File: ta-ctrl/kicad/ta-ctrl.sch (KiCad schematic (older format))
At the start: 25 parts, among them J1 PinSocket_16_ctrl, J2 PinSocket_16_ctrl, J3 MountingHole_ctrl, J4 PinSocket_4_ctrl, J5 PinSocket_4_ctrl, J6 PinSocket_5_ctrl, J7 PinSocket_5_ctrl, U1 LSF0204, U2 LSF0204, U3 LSF0204

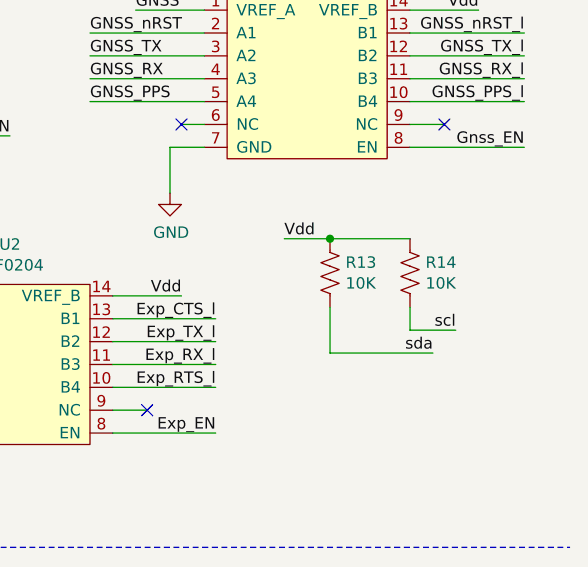
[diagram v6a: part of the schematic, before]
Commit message: updated parts vendors and added BOM
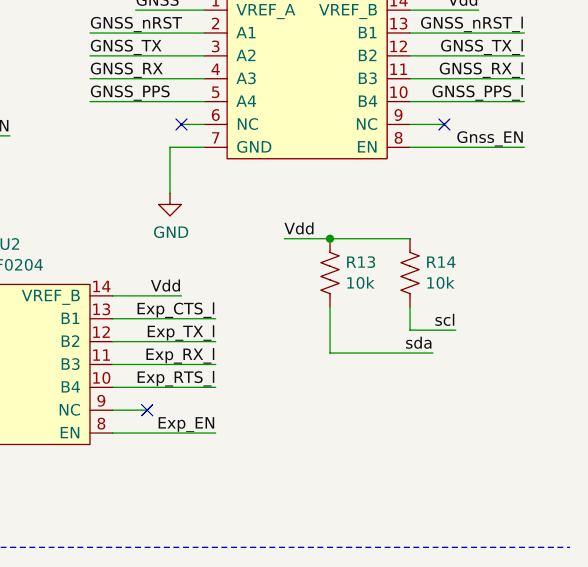
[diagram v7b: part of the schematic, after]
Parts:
- R13, R14: value 10K -> 10k; Manufacturer Part Number (none) -> CRCW060310K0FKEAHP; Vendor (none) -> Digikey; Vendor Part Number (none) -> 541-10.0KSCT-ND
- U1, U2, U3: Manufacturer Part Number (none) -> LSF0204QPWRQ1; Vendor (none) -> Digikey; Vendor Part Number (none) -> 296-51425-1-ND
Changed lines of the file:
@@
 F 2 "ta-ctrl:TSSOP-14" H 6850 1200 50  0001 C CNN
 F 3 "https://www.ti.com/lit/ds/symlink/lsf0204-q1.pdf?HQS=TI-null-null-digikeymode-df-pf-null-wwe&ts=1595462922658" H 6850 1200 50  0001 C CNN
+F 4 "LSF0204QPWRQ1" H 7050 1200 50  0001 C CNN "Manufacturer Part Number"
+F 5 "Digikey" H 7050 1200 50  0001 C CNN "Vendor"
+F 6 "296-51425-1-ND" H 7050 1200 50  0001 C CNN "Vendor Part Number"
 	1    7050 1200
 	1    0    0    -1
@@
 F 2 "ta-ctrl:TSSOP-14" H 9200 1250 50  0001 C CNN
 F 3 "https://www.ti.com/lit/ds/symlink/lsf0204-q1.pdf?HQS=TI-null-null-digikeymode-df-pf-null-wwe&ts=1595462922658" H 9200 1250 50  0001 C CNN
+F 4 "LSF0204QPWRQ1" H 9400 1250 50  0001 C CNN "Manufacturer Part Number"
+F 5 "Digikey" H 9400 1250 50  0001 C CNN "Vendor"
+F 6 "296-51425-1-ND" H 9400 1250 50  0001 C CNN "Vendor Part Number"
 	1    9400 1250
 	1    0    0    -1
@@
 F 2 "ta-ctrl:TSSOP-14" H 7900 2500 50  0001 C CNN
 F 3 "https://www.ti.com/lit/ds/symlink/lsf0204-q1.pdf?HQS=TI-null-null-digikeymode-df-pf-null-wwe&ts=1595462922658" H 7900 2500 50  0001 C CNN
+F 4 "LSF0204QPWRQ1" H 8100 2500 50  0001 C CNN "Manufacturer Part Number"
+F 5 "Digikey" H 8100 2500 50  0001 C CNN "Vendor"
+F 6 "296-51425-1-ND" H 8100 2500 50  0001 C CNN "Vendor Part Number"
 	1    8100 2500
 	1    0    0    -1
@@
 P 9500 2000
 F 0 "R13" H 9568 2046 50  0000 L CNN
-F 1 "10K" H 9568 1955 50  0000 L CNN
+F 1 "10k" H 9568 1955 50  0000 L CNN
 F 2 "ta-ctrl:R_0603_1608Metric_ctrl_cpy" V 9540 1990 50  0001 C CNN
-F 3 "~" H 9500 2000 50  0001 C CNN
+F 3 "https://www.digikey.com/product-detail/en/vishay-dale/CRCW060310K0FKEAHP/541-10-0KSCT-ND/2222780" H 9500 2000 50  0001 C CNN
+F 4 "CRCW060310K0FKEAHP" H 9500 2000 50  0001 C CNN "Manufacturer Part Number"
+F 5 "Digikey" H 9500 2000 50  0001 C CNN "Vendor"
+F 6 "541-10.0KSCT-ND" H 9500 2000 50  0001 C CNN "Vendor Part Number"
 	1    9500 2000
 	1    0    0    -1
@@
 P 9850 2000
 F 0 "R14" H 9918 2046 50  0000 L CNN
-F 1 "10K" H 9918 1955 50  0000 L CNN
+F 1 "10k" H 9918 1955 50  0000 L CNN
 F 2 "ta-ctrl:R_0603_1608Metric_ctrl_cpy" V 9890 1990 50  0001 C CNN
-F 3 "~" H 9850 2000 50  0001 C CNN
+F 3 "https://www.digikey.com/product-detail/en/vishay-dale/CRCW060310K0FKEAHP/541-10-0KSCT-ND/2222780" H 9850 2000 50  0001 C CNN
+F 4 "CRCW060310K0FKEAHP" H 9850 2000 50  0001 C CNN "Manufacturer Part Number"
+F 5 "Digikey" H 9850 2000 50  0001 C CNN "Vendor"
+F 6 "541-10.0KSCT-ND" H 9850 2000 50  0001 C CNN "Vendor Part Number"
 	1    9850 2000
 	1    0    0    -1

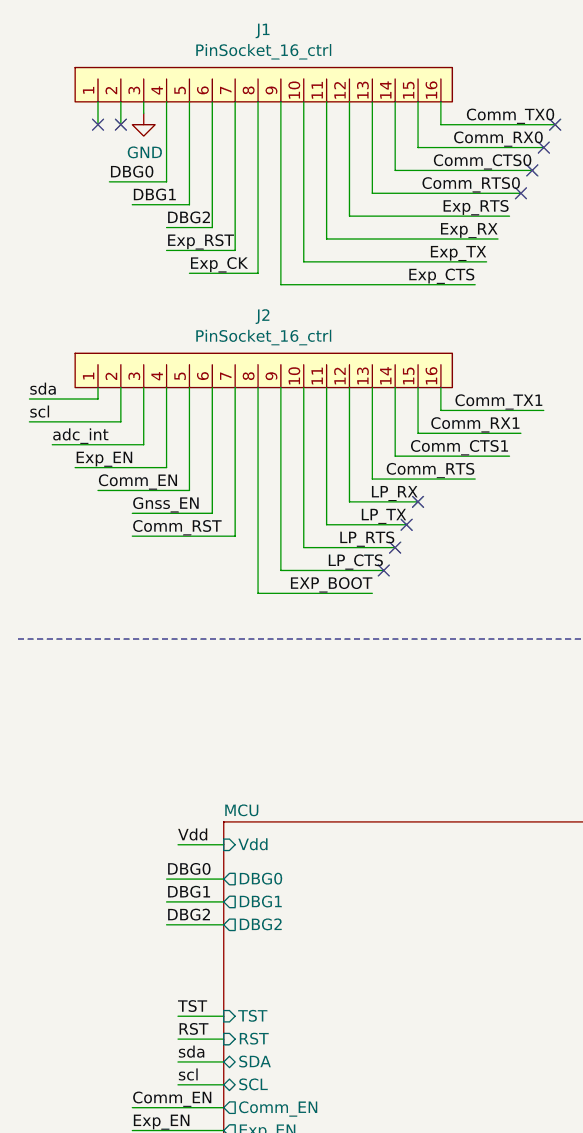
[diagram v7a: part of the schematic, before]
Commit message: deleted fp-info-cache files???
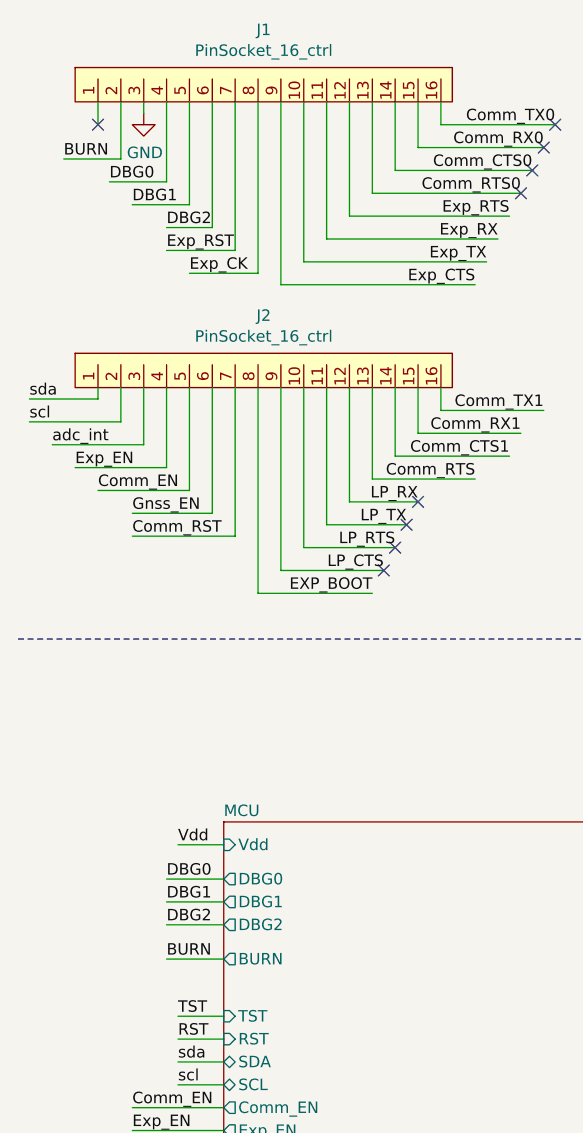
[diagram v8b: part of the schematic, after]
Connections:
- net BURN: now reaches J1.2
- no-connect marks 25 -> 24
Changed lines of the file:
@@
 	950  5850 1400 5850
 NoConn ~ 850  950
-NoConn ~ 950  950
 Wire Wire Line
 	850  850  850  950
-Wire Wire Line
-	950  850  950  950
 Text Label 900  1200 0    50   ~ 0
 DBG0
@@
 F32 "INT_AG" I R 4500 5500 50
 F33 "DEN_AG" I R 4500 5600 50
+F34 "BURN" O L 1400 4600 50
 $EndSheet
 Wire Wire Line
@@
 Wire Wire Line
 	4500 5600 6600 5600
+Text Label 700  1100 0    50   ~ 0
+BURN
+Wire Wire Line
+	950  1100 700  1100
+Wire Wire Line
+	950  850  950  1100
+Text Label 1150 4600 0    50   ~ 0
+BURN
+Wire Wire Line
+	1150 4600 1400 4600
 $EndSCHEMATC
